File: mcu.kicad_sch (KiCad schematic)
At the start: 22 parts, among them J1 SWD_DBG, U1 STM32F405RGTx, Y1 8MHz, Y2 32.768kHz

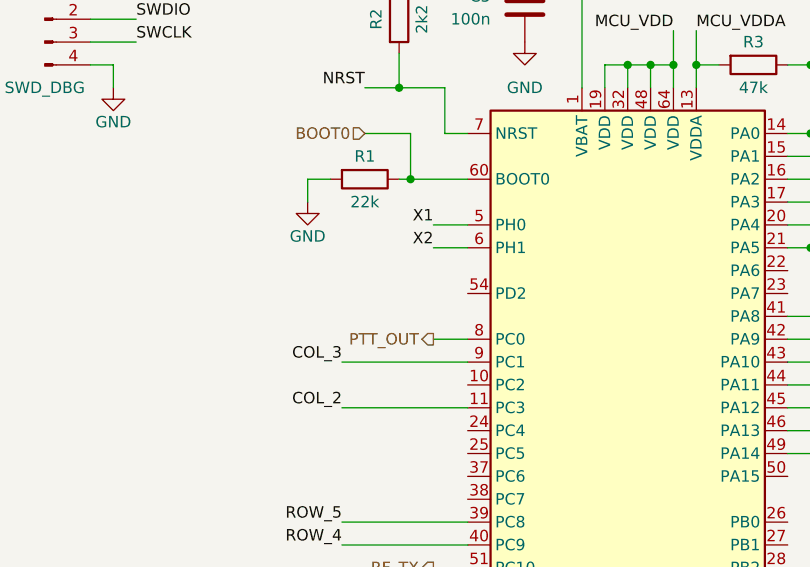
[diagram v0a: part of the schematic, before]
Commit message: routed BTN_OK
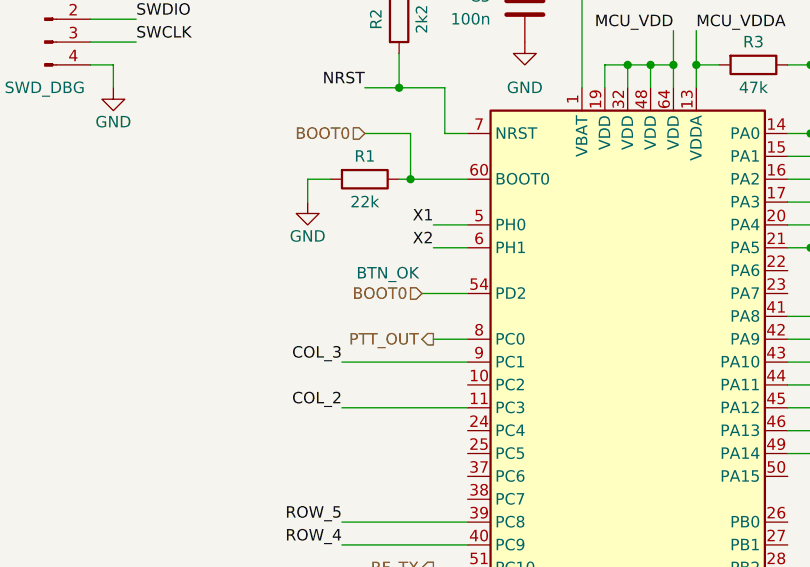
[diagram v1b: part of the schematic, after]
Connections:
- net BOOT0: now also U1.54 (PD2)
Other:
- note added: "BTN_OK"
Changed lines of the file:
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@@
+	(wire
+		(pts
+			(xy 120.65 74.93) (xy 125.73 74.93)
+		)
+		(stroke
+			(width 0)
+			(type default)
+		)
+	)
 	(wire
 		(pts
@@
 		)
 	)
+	(text "BTN_OK"
+		(exclude_from_sim no)
+		(at 116.84 73.66 0)
+		(effects
+			(font
+				(size 1.27 1.27)
+			)
+			(justify bottom)
+		)
+	)
 	(label "MCU_VDD"
 		(at 118.11 38.1 180)
@@
 		(fields_autoplaced yes)
 		(effects
+			(font
+				(size 1.27 1.27)
+			)
+			(justify right)
+		)
+	)
+	(hierarchical_label "BOOT0"
+		(shape input)
+		(at 120.65 74.93 180)
+		(fields_autoplaced yes)
+		(effects

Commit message: PN update
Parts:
- C1, C2: MPN (none) -> 710-885012005039; PN (none) -> 710-885012005039
- C10, C5, C6, C7, C8, C9: MPN (none) -> 810-CGA2B3X7R1H104KB; PN (none) -> 810-CGA2B3X7R1H104KB
- C3, C4: MPN (none) -> 963-LMK105BJ225MV-F; PN (none) -> 963-LMK105BJ225MV-F
- J1, Y2: now not fitted
- R1, R6: MPN (none) -> 279-CRGCQ0402J22K; PN (none) -> 279-CRGCQ0402J22K
- R2: MPN (none) -> 279-CRGCQ0402J2K2; PN (none) -> 279-CRGCQ0402J2K2
- R3, R4: MPN (none) -> 652-CR0402JW-473GLF; PN (none) -> 652-CR0402JW-473GLF
- R5: MPN (none) -> 603-RC0402JR-7D10KL; PN (none) -> 603-RC0402JR-7D10KL
- U1: MPN (none) -> 511-STM32F405RGT6; PN (none) -> 511-STM32F405RGT6
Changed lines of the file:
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@@
 			)
 		)
-		(property "PN" ""
+		(property "PN" "279-CRGCQ0402J22K"
 			(at 114.3 62.23 0)
 			(effects
@@
 			)
 		)
-		(property "MPN" ""
+		(property "MPN" "279-CRGCQ0402J22K"
 			(at 114.3 62.23 0)
 			(effects
@@
 			)
 		)
+		(property "MPN" "810-CGA2B3X7R1H104KB"
+			(at 132.08 43.18 0)
+			(effects
+				(font
+					(size 1.27 1.27)
+				)
+				(hide yes)
+			)
+		)
+		(property "PN" "810-CGA2B3X7R1H104KB"
+			(at 132.08 43.18 0)
+			(effects
+				(font
+					(size 1.27 1.27)
+				)
+				(hide yes)
+			)
+		)
 		(pin "1"
 		)
@@
 			)
 		)
-		(property "PN" ""
+		(property "PN" "710-885012005039"
 			(at 55.88 45.72 0)
 			(effects
@@
 			)
 		)
-		(property "MPN" ""
+		(property "MPN" "710-885012005039"
 			(at 55.88 45.72 0)
 			(effects
@@
 			)
 		)
-		(property "PN" ""
+		(property "PN" "603-RC0402JR-7D10KL"
 			(at 181.61 72.39 0)
 			(effects
@@
 			)
 		)
-		(property "MPN" ""
+		(property "MPN" "603-RC0402JR-7D10KL"
 			(at 181.61 72.39 0)
 			(effects
@@
 			)
 		)
-		(property "PN" ""
+		(property "PN" "963-LMK105BJ225MV-F"
 			(at 119.38 137.16 0)
 			(effects
@@
 			)
 		)
-		(property "MPN" ""
+		(property "MPN" "963-LMK105BJ225MV-F"
 			(at 119.38 137.16 0)
 			(effects
@@
 			)
 		)
+		(property "MPN" "810-CGA2B3X7R1H104KB"
+			(at 231.14 46.99 0)
+			(effects
+				(font
+					(size 1.27 1.27)
+				)
+				(hide yes)
+			)
+		)
+		(property "PN" "810-CGA2B3X7R1H104KB"
+			(at 231.14 46.99 0)
+			(effects
+				(font
+					(size 1.27 1.27)
+				)
+				(hide yes)
+			)
+		)
 		(pin "1"
 		)
@@
 			)
 		)
-		(property "PN" ""
+		(property "PN" "652-CR0402JW-473GLF"
 			(at 170.18 49.53 0)
 			(effects
@@
 			)
 		)
-		(property "MPN" ""
+		(property "MPN" "652-CR0402JW-473GLF"
 			(at 170.18 49.53 0)
 			(effects
@@
 			)
 		)
+		(property "MPN" "511-STM32F405RGT6"
+			(at 143.51 100.33 0)
+			(effects
+				(font
+					(size 1.27 1.27)
+				)
+				(hide yes)
+			)
+		)
+		(property "PN" "511-STM32F405RGT6"
+			(at 143.51 100.33 0)
+			(effects
+				(font
+					(size 1.27 1.27)
+				)
+				(hide yes)
+			)
+		)
 		(pin "39"
 		)
@@
 			)
 		)
+		(property "MPN" "810-CGA2B3X7R1H104KB"
+			(at 242.57 46.99 0)
+			(effects
+				(font
+					(size 1.27 1.27)
+				)
+				(hide yes)
+			)
+		)
+		(property "PN" "810-CGA2B3X7R1H104KB"
+			(at 242.57 46.99 0)
+			(effects
+				(font
+					(size 1.27 1.27)
+				)
+				(hide yes)
+			)
+		)
 		(pin "1"
 		)
@@
 		(in_bom yes)
 		(on_board yes)
-		(dnp no)
+		(dnp yes)
 		(fields_autoplaced yes)
 		(property "Reference" "Y2"
@@
 			)
 		)
-		(property "PN" ""
+		(property "PN" "652-CR0402JW-473GLF"
 			(at 157.48 49.53 0)
 			(effects
@@
 			)
 		)
-		(property "MPN" ""
+		(property "MPN" "652-CR0402JW-473GLF"
 			(at 157.48 49.53 0)
 			(effects
@@
 			)
 		)
+		(property "MPN" "810-CGA2B3X7R1H104KB"
+			(at 219.71 46.99 0)
+			(effects
+				(font
+					(size 1.27 1.27)
+				)
+				(hide yes)
+			)
+		)
+		(property "PN" "810-CGA2B3X7R1H104KB"
+			(at 219.71 46.99 0)
+			(effects
+				(font
+					(size 1.27 1.27)
+				)
+				(hide yes)
+			)
+		)
 		(pin "1"
 		)
@@
 		(in_bom yes)
 		(on_board yes)
-		(dnp no)
+		(dnp yes)
 		(property "Reference" "J1"
 			(at 78.74 39.37 0)
@@
 			)
 		)
+		(property "MPN" "810-CGA2B3X7R1H104KB"
+			(at 254 46.99 0)
+			(effects
+				(font
+					(size 1.27 1.27)
+				)
+				(hide yes)
+			)
+		)
+		(property "PN" "810-CGA2B3X7R1H104KB"
+			(at 254 46.99 0)
+			(effects
+				(font
+					(size 1.27 1.27)
+				)
+				(hide yes)
+			)
+		)
 		(pin "1"
 		)
@@
 			)
 		)
+		(property "MPN" "810-CGA2B3X7R1H104KB"
+			(at 265.43 46.99 0)
+			(effects
+				(font
+					(size 1.27 1.27)
+				)
+				(hide yes)
+			)
+		)
+		(property "PN" "810-CGA2B3X7R1H104KB"
+			(at 265.43 46.99 0)
+			(effects
+				(font
+					(size 1.27 1.27)
+				)
+				(hide yes)
+			)
+		)
 		(pin "1"
 		)
@@
 			)
 		)
-		(property "PN" ""
+		(property "PN" "963-LMK105BJ225MV-F"
 			(at 107.95 137.16 0)
 			(effects
@@
 			)
 		)
-		(property "MPN" ""
+		(property "MPN" "963-LMK105BJ225MV-F"
 			(at 107.95 137.16 0)
 			(effects
@@
 			)
 		)
-		(property "PN" ""
+		(property "PN" "279-CRGCQ0402J2K2"
 			(at 118.11 44.45 0)
 			(effects
@@
 			)
 		)
-		(property "MPN" ""
+		(property "MPN" "279-CRGCQ0402J2K2"
 			(at 118.11 44.45 0)
 			(effects
@@
 			)
 		)
-		(property "PN" ""
+		(property "PN" "710-885012005039"
 			(at 43.18 45.72 0)
 			(effects
@@
 			)
 		)
-		(property "MPN" ""
+		(property "MPN" "710-885012005039"
 			(at 43.18 45.72 0)
 			(effects
@@
 			)
 		)
-		(property "PN" ""
+		(property "PN" "279-CRGCQ0402J22K"
 			(at 181.61 105.41 0)
 			(effects
@@
 			)
 		)
-		(property "MPN" ""
+		(property "MPN" "279-CRGCQ0402J22K"
 			(at 181.61 105.41 0)
 			(effects
